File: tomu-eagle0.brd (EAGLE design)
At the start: 13.2 x 11.7 mm, 21 parts, among them U1 EFM32HG309F64G, X1 USBPCB

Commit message: added first pass at touch sensors
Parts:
- removed 0A, 0B, 1A, 1B: TPTP08R, testpad:TP08R
- removed X1: USBPCB, usb:USB-A-PCB
- added U$1: USBPCB2, todstuff:USB-A-PCB-2
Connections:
- net CAP0A: no longer 0A.TP
- net CAP0B: no longer 0B.TP
- net CAP1A: no longer 1A.TP
- net CAP1B: no longer 1B.TP
- net GND: now also U$1.GND; no longer X1.GND
- net USB_D+: now also U$1.USB_P; no longer X1.USB_P
- net USB_D-: now also U$1.USB_M; no longer X1.USB_M
- net VUSB: now also U$1.5V; no longer X1.5V
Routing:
- net VUSB: track 9.58 -> 6.93 mm
- net +3V3: track 9.24 -> 10.9 mm
- net GND: track 23.0 -> 22.4 mm
- net CAP0A: track 3.34 -> 3.63 mm, vias 0 -> 2
- net CAP0B: track 6.86 -> 7.12 mm, vias 0 -> 2
- net CAP1A: track 3.42 -> 3.39 mm, vias 0 -> 2
- net CAP1B: vias 2 -> 3
- added copper zone on layer 1, net CAP0A
- added copper zone on layer 16, net CAP0A
- added copper zone on layer 1, net CAP0B
- added copper zone on layer 16, net CAP0B
- added copper zone on layer 1, net CAP1A
- added copper zone on layer 16, net CAP1A
- added copper zone on layer 1, net CAP1B
- added copper zone on layer 16, net CAP1B
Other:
- board size 13.2 x 11.7 mm -> 13.2 x 11.2 mm

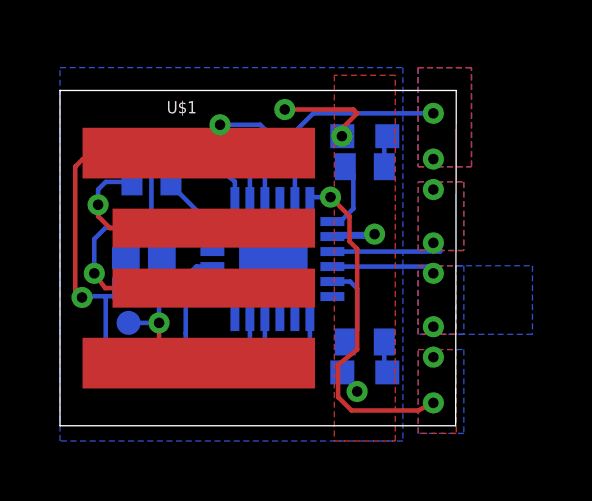
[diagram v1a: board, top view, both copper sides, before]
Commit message: fixed up touch sensor
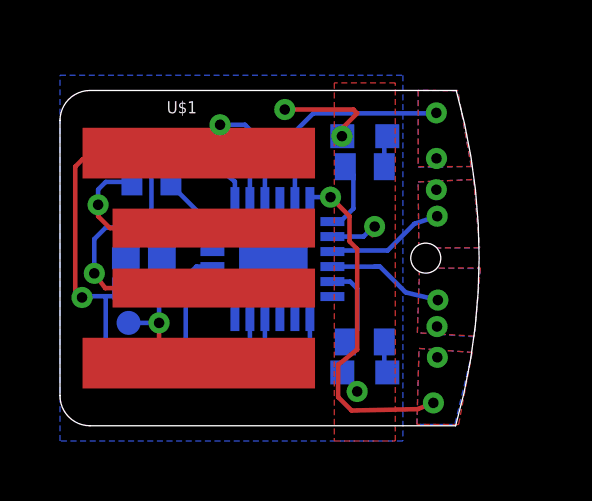
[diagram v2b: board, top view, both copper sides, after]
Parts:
- moved U1 0.72 mm to (7.11, 5.84)
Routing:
- net +3V3: track 10.9 -> 9.43 mm
- net CAP1A: track 3.39 -> 4.08 mm
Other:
- board size 13.2 x 11.2 mm -> 14 x 11.2 mm
